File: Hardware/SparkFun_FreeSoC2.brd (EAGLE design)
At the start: 116.8 x 53.3 mm, 108 parts, among them U1 CY8C5888AXI-LP096, U2 MIC5219 5V, U3 MIC5219 3.3V, U4 2A/20V, U7 CY8C5868LTI-LP039, Y1 32.768kHz

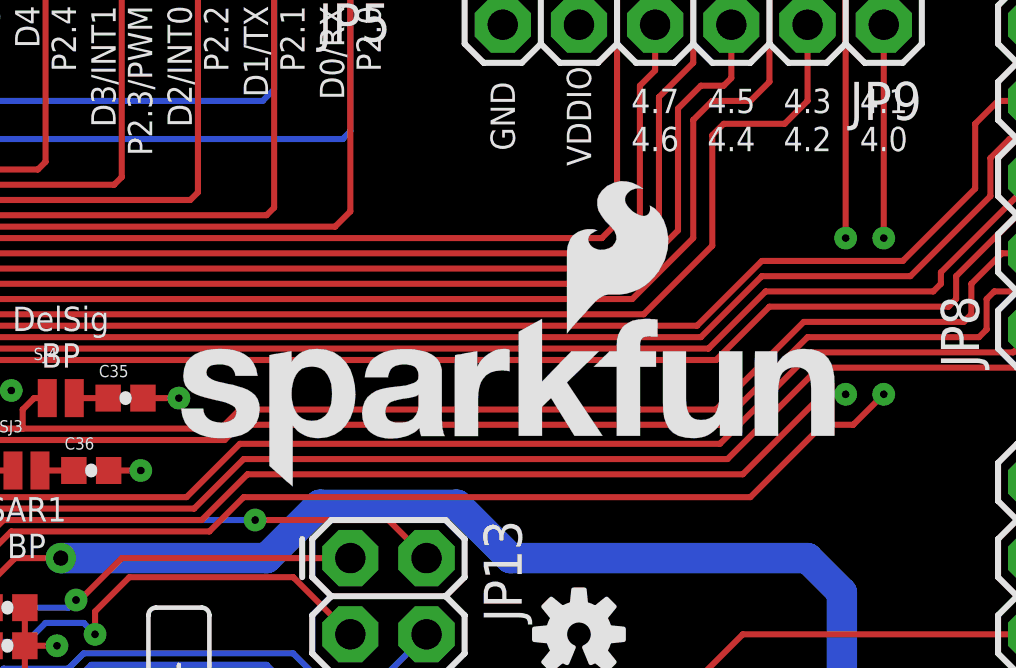
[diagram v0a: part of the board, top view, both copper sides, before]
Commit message: Enthickened lines on logos for better rendering
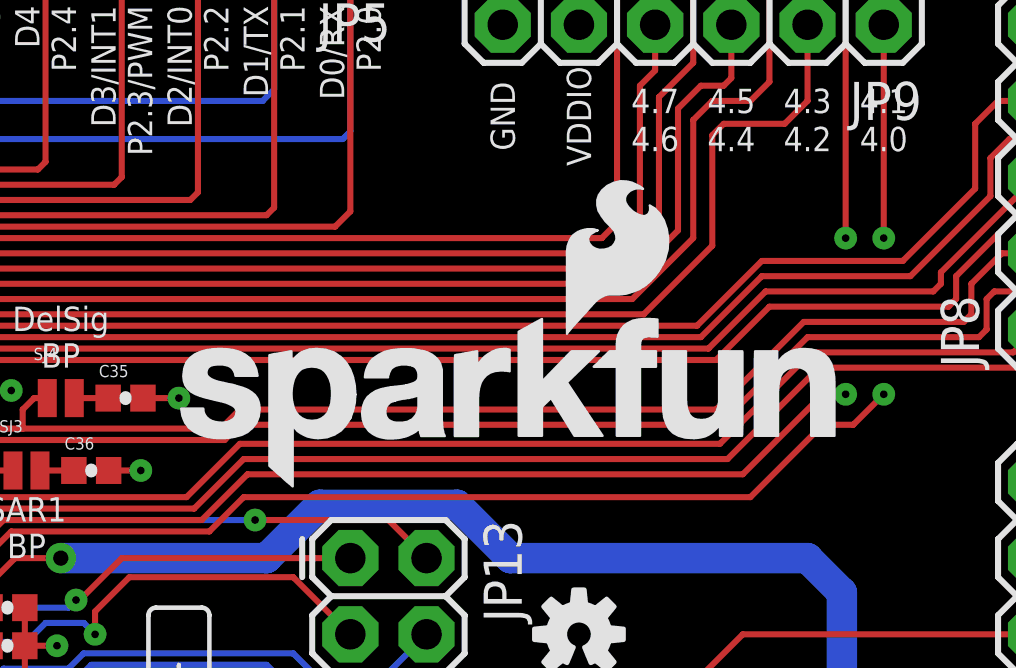
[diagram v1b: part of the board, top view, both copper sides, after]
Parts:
- FRAME1, FRAME2, FRAME3: value (none) -> FRAME-LETTERNO_PACKAGE
- U$2: device SparkFun-Aesthetics:CREATIVE_COMMONS -> SparkFun-Aesthetics:CREATIVE_COMMONS@1
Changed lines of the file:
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@@
 <element name="SJ6" library="SparkFun-Passives" package="PAD-JUMPER-2-NO_NO_SILK" value="JUMPER-PAD-2-NO" x="43.18" y="43.815" rot="R180"/>
 <element name="SJ7" library="SparkFun-Passives" package="PAD-JUMPER-2-NO_NO_SILK" value="JUMPER-PAD-2-NO" x="43.18" y="41.91" rot="R180"/>
-<element name="FRAME1" library="SparkFun-Aesthetics" package="DUMMY" value="" x="-15.24" y="-15.24">
+<element name="FRAME1" library="SparkFun-Aesthetics" package="DUMMY" value="FRAME-LETTERNO_PACKAGE" x="-15.24" y="-15.24">
 <attribute name="VERSION" value="v01" x="-15.24" y="-15.24" size="1.778" layer="27" font="vector" ratio="15" display="off"/>
 <attribute name="DESIGNER" value="Nobody" x="-15.24" y="-15.24" size="1.778" layer="27" font="vector" ratio="15" display="off"/>
 </element>
-<element name="FRAME2" library="SparkFun-Aesthetics" package="DUMMY" value="" x="-15.24" y="-16.51">
+<element name="FRAME2" library="SparkFun-Aesthetics" package="DUMMY" value="FRAME-LETTERNO_PACKAGE" x="-15.24" y="-16.51">
 <attribute name="VERSION" value="v01" x="-15.24" y="-16.51" size="1.778" layer="27" font="vector" ratio="15" display="off"/>
 <attribute name="DESIGNER" value="Nobody" x="-15.24" y="-16.51" size="1.778" layer="27" font="vector" ratio="15" display="off"/>
 </element>
-<element name="FRAME3" library="SparkFun-Aesthetics" package="DUMMY" value="" x="-15.24" y="-17.78">
+<element name="FRAME3" library="SparkFun-Aesthetics" package="DUMMY" value="FRAME-LETTERNO_PACKAGE" x="-15.24" y="-17.78">
 <attribute name="VERSION" value="v01" x="-15.24" y="-17.78" size="1.778" layer="27" font="vector" ratio="15" display="off"/>
 <attribute name="DESIGNER" value="Nobody" x="-15.24" y="-17.78" size="1.778" layer="27" font="vector" ratio="15" display="off"/>
 </element>
-<element name="U$2" library="SparkFun-Aesthetics" package="CREATIVE_COMMONS" value="" x="35.56" y="-27.94"/>
+<element name="U$2" library="SparkFun-Aesthetics" package="CREATIVE_COMMONS@1" value="" x="35.56" y="-27.94"/>
 <element name="C18" library="SparkFun-Capacitors" package="CAP-PTH-SMALL" value="" x="80.645" y="22.86" rot="R90"/>
 <element name="C24" library="SparkFun-Capacitors" package="CAP-PTH-SMALL" value="" x="75.565" y="22.86" rot="R90"/>

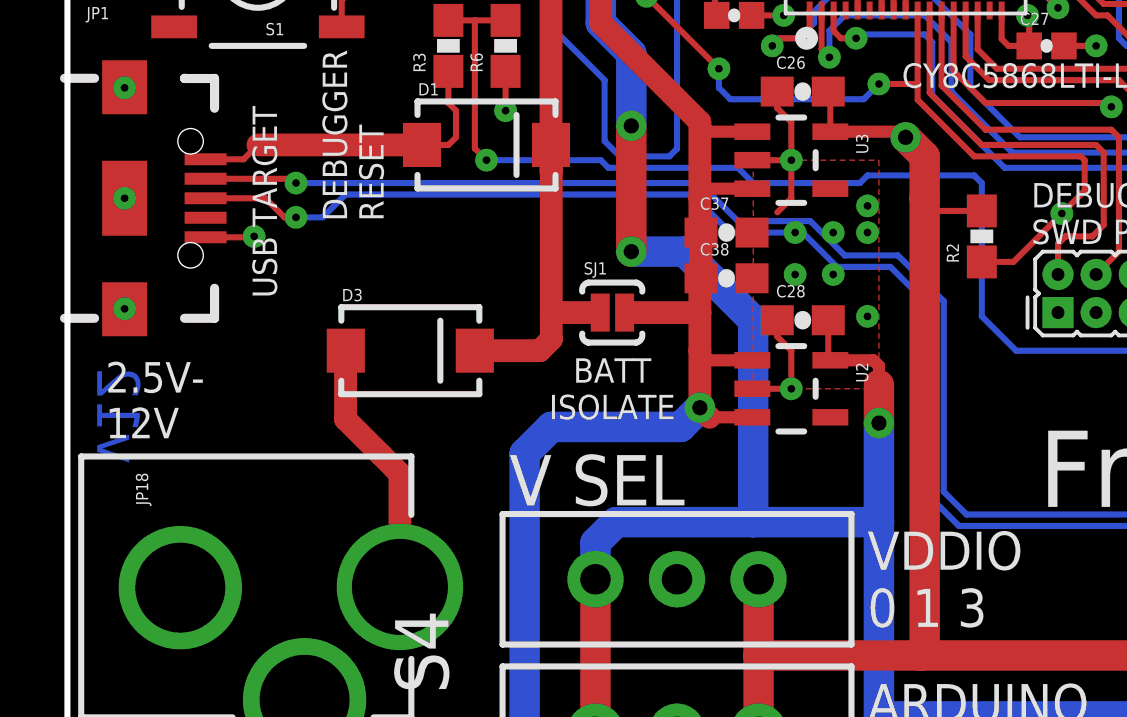
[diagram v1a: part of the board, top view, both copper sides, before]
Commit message: Chg to V13, fix traces over vias
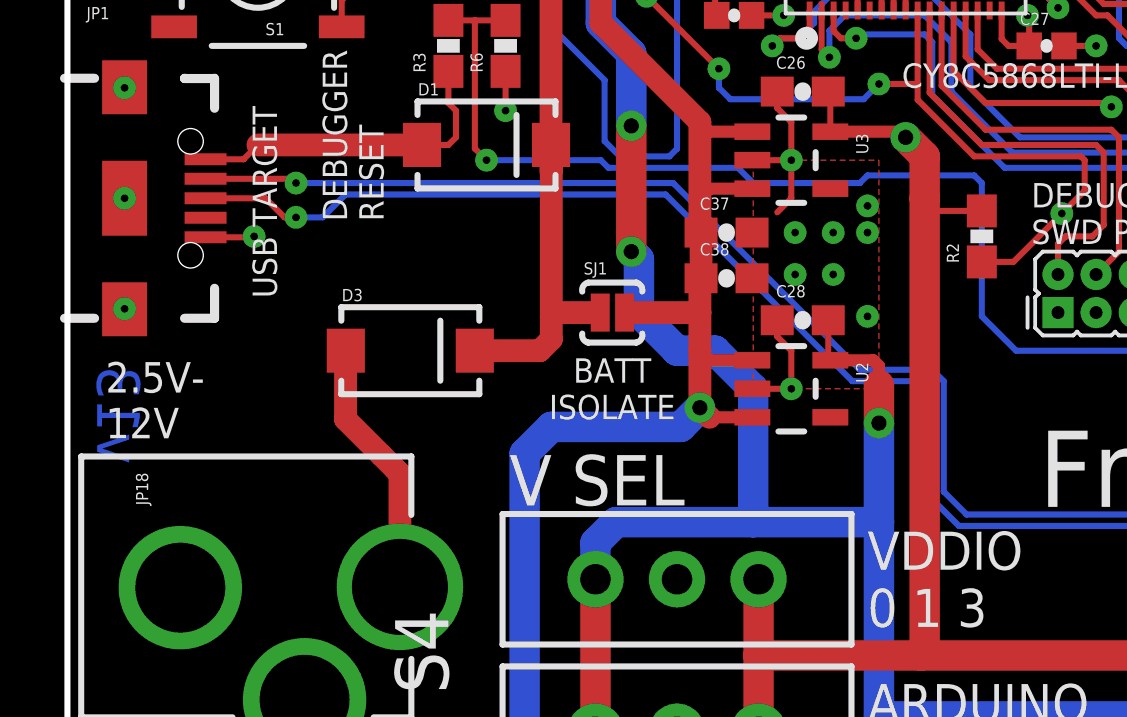
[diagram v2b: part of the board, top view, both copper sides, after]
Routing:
- net PSOC_D+_BUS: track 61.1 -> 59.5 mm
- net PSOC_D-_BUS: track 59.2 -> 57.6 mm
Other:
- board text added: "v13"
- board text removed: "v12"
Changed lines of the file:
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@@
 <grid distance="0.05" unitdist="inch" unit="inch" style="lines" multiple="1" display="yes" altdistance="0.005" altunitdist="inch" altunit="inch"/>
 <layers>
-<layer number="1" name="Top" color="4" fill="1" visible="yes" active="yes"/>
+<layer number="1" name="Top" color="4" fill="1" visible="no" active="yes"/>
 <layer number="2" name="Route2" color="1" fill="3" visible="no" active="yes"/>
 <layer number="15" name="Route15" color="4" fill="6" visible="no" active="yes"/>
 <layer number="16" name="Bottom" color="1" fill="1" visible="yes" active="yes"/>
-<layer number="17" name="Pads" color="2" fill="1" visible="yes" active="yes"/>
+<layer number="17" name="Pads" color="2" fill="1" visible="no" active="yes"/>
 <layer number="18" name="Vias" color="2" fill="1" visible="yes" active="yes"/>
-<layer number="19" name="Unrouted" color="6" fill="1" visible="yes" active="yes"/>
-<layer number="20" name="Dimension" color="15" fill="1" visible="yes" active="yes"/>
-<layer number="21" name="tPlace" color="16" fill="1" visible="yes" active="yes"/>
-<layer number="22" name="bPlace" color="14" fill="1" visible="yes" active="yes"/>
-<layer number="23" name="tOrigins" color="15" fill="1" visible="yes" active="yes"/>
-<layer number="24" name="bOrigins" color="15" fill="1" visible="yes" active="yes"/>
+<layer number="19" name="Unrouted" color="6" fill="1" visible="no" active="yes"/>
+<layer number="20" name="Dimension" color="15" fill="1" visible="no" active="yes"/>
+<layer number="21" name="tPlace" color="16" fill="1" visible="no" active="yes"/>
+<layer number="22" name="bPlace" color="14" fill="1" visible="no" active="yes"/>
+<layer number="23" name="tOrigins" color="15" fill="1" visible="no" active="yes"/>
+<layer number="24" name="bOrigins" color="15" fill="1" visible="no" active="yes"/>
 <layer number="25" name="tNames" color="7" fill="1" visible="no" active="yes"/>
 <layer number="26" name="bNames" color="7" fill="1" visible="no" active="yes"/>
@@
 <layer number="43" name="vRestrict" color="2" fill="10" visible="no" active="yes"/>
 <layer number="44" name="Drills" color="7" fill="1" visible="no" active="yes"/>
-<layer number="45" name="Holes" color="7" fill="1" visible="yes" active="yes"/>
+<layer number="45" name="Holes" color="7" fill="1" visible="no" active="yes"/>
 <layer number="46" name="Milling" color="3" fill="1" visible="no" active="yes"/>
 <layer number="47" name="Measures" color="7" fill="1" visible="no" active="yes"/>
-<layer number="51" name="tDocu" color="6" fill="1" visible="yes" active="yes"/>
+<layer number="51" name="tDocu" color="6" fill="1" visible="no" active="yes"/>
 <layer number="52" name="bDocu" color="7" fill="1" visible="no" active="no"/>
 <layer number="3" name="Route3" color="4" fill="3" visible="no" active="no"/>
@@
 <text x="54.737" y="35.814" size="0.8128" layer="21" font="vector" ratio="15">CY8C5888AXI-LP096</text>
 <text x="27.813" y="26.543" size="0.8128" layer="21" font="vector" ratio="15">CY8C5868LTI-LP039</text>
-<text x="2.413" y="17.272" size="1.4224" layer="16" font="vector" ratio="15" rot="MR270">v12</text>
+<text x="2.413" y="17.272" size="1.4224" layer="16" font="vector" ratio="15" rot="MR270">v13</text>
 <text x="62.23" y="-27.94" size="1.778" layer="51" ratio="15">Mike Hord</text>
 <text x="1.651" y="44.196" size="1.016" layer="21" font="vector" ratio="15">2.5V-
@@
 <wire x1="7.62" y1="22.225" x2="8.509" y2="22.225" width="0.2032" layer="16"/>
 <wire x1="8.509" y1="22.225" x2="9.271" y2="22.987" width="0.2032" layer="16"/>
-<wire x1="9.271" y1="22.987" x2="20.828" y2="22.987" width="0.2032" layer="16"/>
-<wire x1="20.828" y1="22.987" x2="22.098" y2="21.717" width="0.2032" layer="16"/>
-<wire x1="22.098" y1="21.717" x2="24.511" y2="21.717" width="0.2032" layer="16"/>
-<wire x1="24.511" y1="21.717" x2="25.654" y2="20.574" width="0.2032" layer="16"/>
-<wire x1="25.654" y1="20.574" x2="27.432" y2="20.574" width="0.2032" layer="16"/>
-<wire x1="27.432" y1="20.574" x2="28.829" y2="19.177" width="0.2032" layer="16"/>
-<wire x1="28.829" y1="19.177" x2="28.829" y2="12.827" width="0.2032" layer="16"/>
+<wire x1="9.271" y1="22.987" x2="19.939" y2="22.987" width="0.2032" layer="16"/>
+<wire x1="28.829" y1="16.383" x2="28.829" y2="12.827" width="0.2032" layer="16"/>
 <wire x1="28.829" y1="12.827" x2="29.718" y2="11.938" width="0.2032" layer="16"/>
 <wire x1="29.718" y1="11.938" x2="51.943" y2="11.938" width="0.2032" layer="16"/>
@@
 <wire x1="53.34" y1="13.208" x2="53.467" y2="13.335" width="0.2032" layer="16"/>
 <wire x1="53.467" y1="13.335" x2="54.229" y2="13.335" width="0.2032" layer="16"/>
+<wire x1="19.939" y1="22.987" x2="26.162" y2="16.764" width="0.2032" layer="16"/>
+<wire x1="26.162" y1="16.764" x2="28.448" y2="16.764" width="0.2032" layer="16"/>
+<wire x1="28.448" y1="16.764" x2="28.829" y2="16.383" width="0.2032" layer="16"/>
 </signal>
 <signal name="PSOC_D-_BUS">
@@
 <wire x1="7.478" y1="23.51" x2="7.62" y2="23.368" width="0.2032" layer="1"/>
 <via x="7.62" y="23.368" extent="1-16" drill="0.254"/>
-<wire x1="7.62" y1="23.368" x2="21.082" y2="23.368" width="0.2032" layer="16"/>
-<wire x1="21.082" y1="23.368" x2="22.352" y2="22.098" width="0.2032" layer="16"/>
-<wire x1="22.352" y1="22.098" x2="24.765" y2="22.098" width="0.2032" layer="16"/>
-<wire x1="24.765" y1="22.098" x2="25.908" y2="20.955" width="0.2032" layer="16"/>
-<wire x1="25.908" y1="20.955" x2="27.686" y2="20.955" width="0.2032" layer="16"/>
-<wire x1="27.686" y1="20.955" x2="29.21" y2="19.431" width="0.2032" layer="16"/>
-<wire x1="29.21" y1="19.431" x2="29.21" y2="13.081" width="0.2032" layer="16"/>
+<wire x1="7.62" y1="23.368" x2="20.193" y2="23.368" width="0.2032" layer="16"/>
+<wire x1="29.21" y1="16.764" x2="29.21" y2="13.081" width="0.2032" layer="16"/>
 <wire x1="29.21" y1="13.081" x2="29.972" y2="12.319" width="0.2032" layer="16"/>
 <wire x1="29.972" y1="12.319" x2="52.578" y2="12.319" width="0.2032" layer="16"/>
@@
 <wire x1="54.102" y1="12.319" x2="54.356" y2="12.065" width="0.2032" layer="1"/>
 <wire x1="54.356" y1="12.065" x2="55.3" y2="12.065" width="0.2032" layer="1"/>
+<wire x1="26.416" y1="17.145" x2="28.829" y2="17.145" width="0.2032" layer="16"/>
+<wire x1="28.829" y1="17.145" x2="29.21" y2="16.764" width="0.2032" layer="16"/>
+<wire x1="26.416" y1="17.145" x2="20.193" y2="23.368" width="0.2032" layer="16"/>
 </signal>
 <signal name="DEBUG_D+_BUS">
@@
 <wire x1="74.168" y1="30.48" x2="72.644" y2="30.48" width="0.2032" layer="1"/>
 <wire x1="72.644" y1="30.48" x2="71.755" y2="29.591" width="0.2032" layer="1"/>
-<wire x1="22.86" y1="12.065" x2="22.86" y2="18.796" width="1.016" layer="16"/>
-<wire x1="22.86" y1="18.796" x2="20.574" y2="21.082" width="1.016" layer="16"/>
-<wire x1="20.574" y1="21.082" x2="18.796" y2="21.082" width="1.016" layer="16"/>
+<wire x1="22.86" y1="12.065" x2="22.86" y2="16.51" width="1.016" layer="16"/>
 <via x="18.796" y="21.082" extent="1-16" drill="0.508"/>
 <wire x1="18.796" y1="21.082" x2="18.796" y2="25.273" width="1.016" layer="1"/>
@@
 <wire x1="71.81" y1="29.155" x2="71.755" y2="29.21" width="0.2032" layer="1"/>
 <wire x1="56.642" y1="6.731" x2="55.499" y2="5.588" width="1.016" layer="16"/>
+<wire x1="22.86" y1="16.51" x2="21.59" y2="17.78" width="1.016" layer="16"/>
+<wire x1="21.59" y1="17.78" x2="20.32" y2="17.78" width="1.016" layer="16"/>
+<wire x1="20.32" y1="17.78" x2="19.05" y2="19.05" width="1.016" layer="16"/>
+<wire x1="19.05" y1="19.05" x2="19.05" y2="20.828" width="1.016" layer="16"/>
+<wire x1="19.05" y1="20.828" x2="18.796" y2="21.082" width="1.016" layer="16"/>
 </signal>
 <signal name="DEBUG_LED">

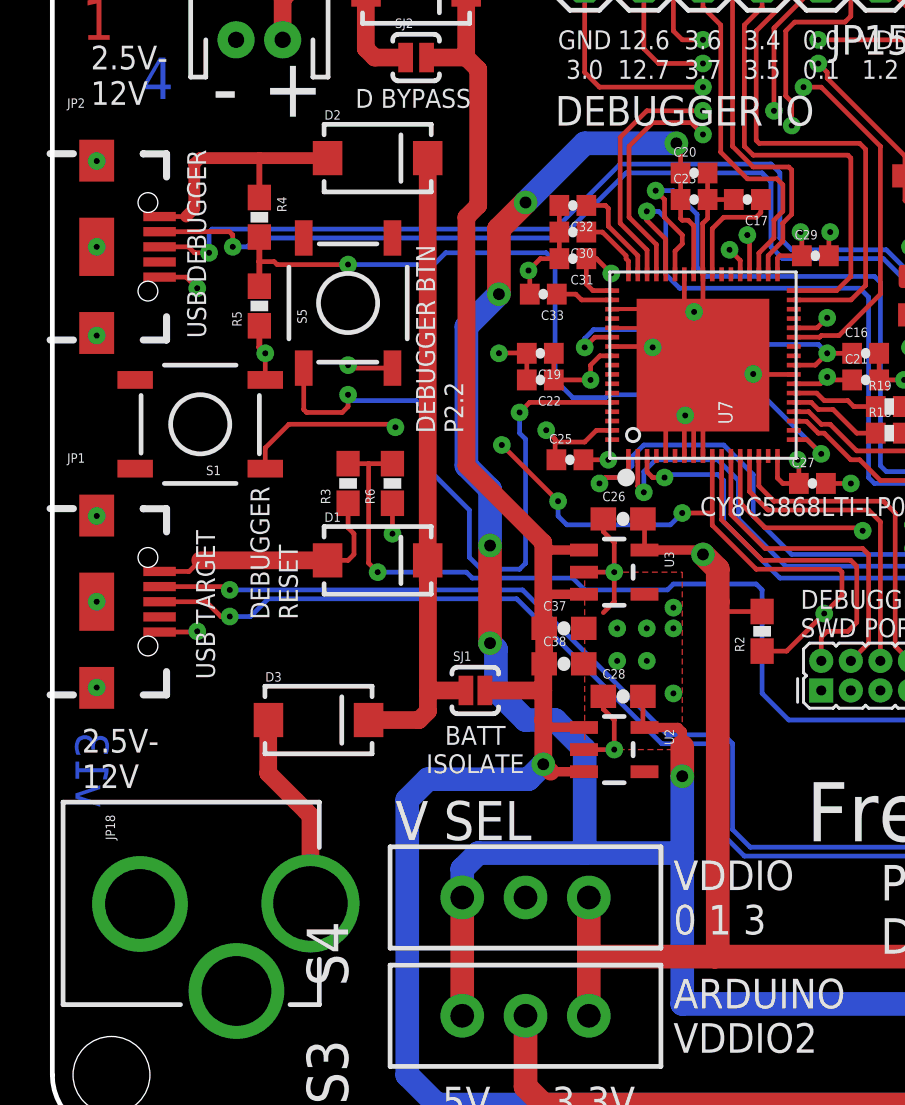
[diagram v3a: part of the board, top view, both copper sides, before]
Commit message: Add small series resistor on regulator bypass caps
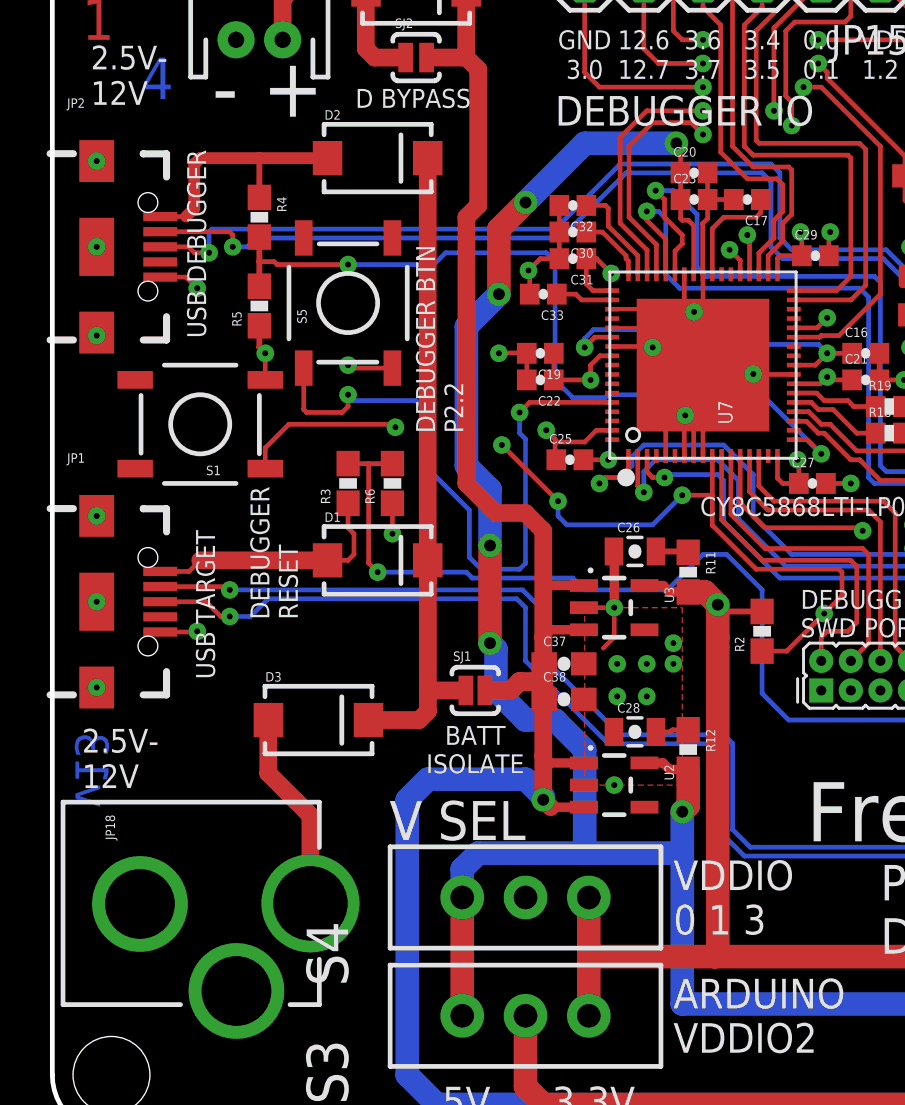
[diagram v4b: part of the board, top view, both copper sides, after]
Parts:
- added R11, R12: 0.27, SparkFun-Resistors:0603-RES
- C26, C28: value 2.2uF -> 10uF; device SparkFun-Capacitors:0603-CAP -> SparkFun-Capacitors:0805-CAP
- JP3: value M02JST-PTH-2 -> (none)
- R10, R20, R21, R9: device SparkFun-Resistors:0603-RES -> SparkFun-Resistors:0603-RES@1
- moved C28 1.61 mm to (25.0, 17.3)
- moved C38 1.52 mm to (22.0, 18.7)
- moved U2 1.52 mm to (24.1, 15.0)
- moved C37 1.52 mm to (22.0, 20.2)
- moved U3 1.52 mm to (24.1, 22.6)
- moved C26 1.49 mm to (25.0, 25.0)
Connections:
- new net N$1: C26.2, R11.1
- new net N$6: C28.2, R12.1
- net 3.3V: now also R11.2; no longer C26.2
- net 5V: now also R12.2; no longer C28.2
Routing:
- net GND: track 127.6 -> 123.7 mm, vias 48 -> 47
- net V_IN: track 119.3 -> 122.6 mm
- net 5V: track 214.4 -> 211.9 mm
- net N$6: track 0.00 -> 1.42 mm
- net N$1: track 0.00 -> 1.40 mm
- net PSOC_D+_BUS: track 59.5 -> 60.8 mm
- net PSOC_D-_BUS: track 57.6 -> 58.8 mm
- net V_BUS_HOST: track 63.2 -> 64.3 mm
